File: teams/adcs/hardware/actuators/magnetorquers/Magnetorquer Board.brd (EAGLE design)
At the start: 90 x 90 mm, 29 parts

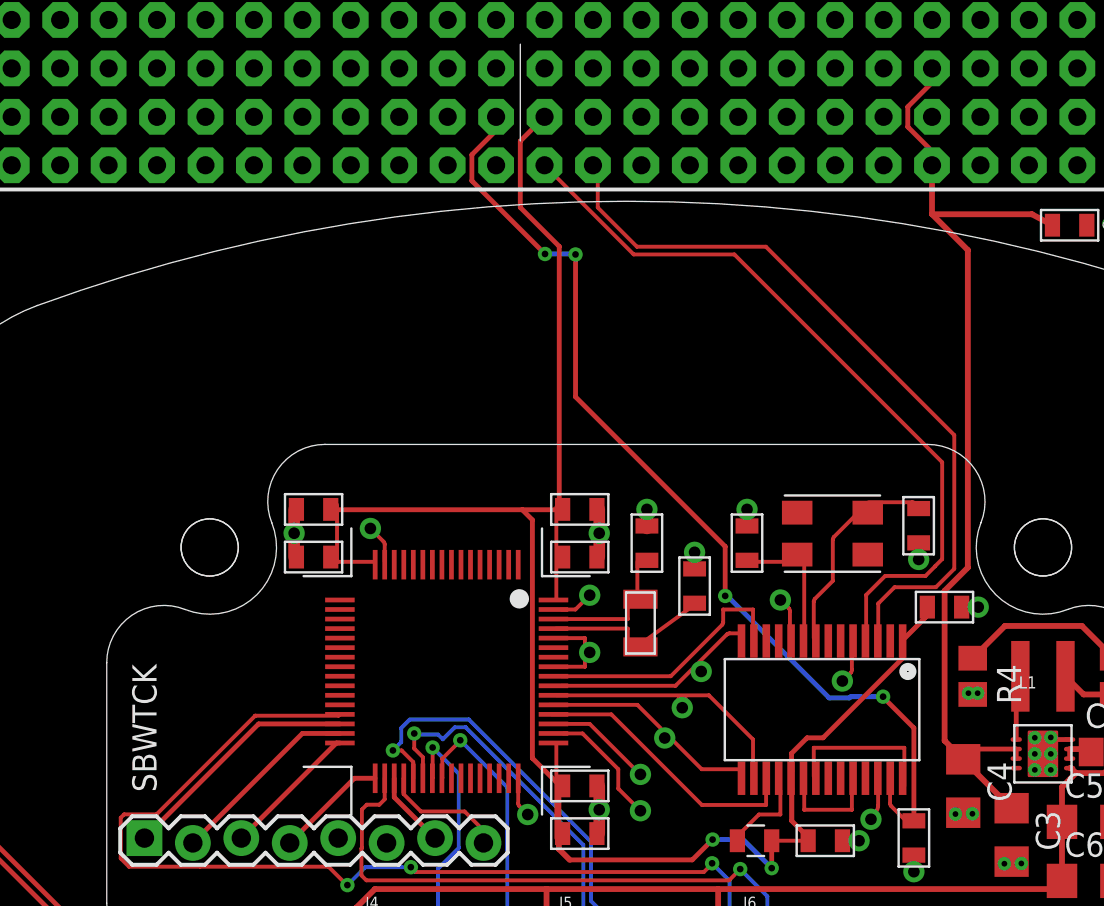
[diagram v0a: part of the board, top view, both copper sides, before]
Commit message: ADCS/MT: Switched from distributed 3V3/5V to LDOs
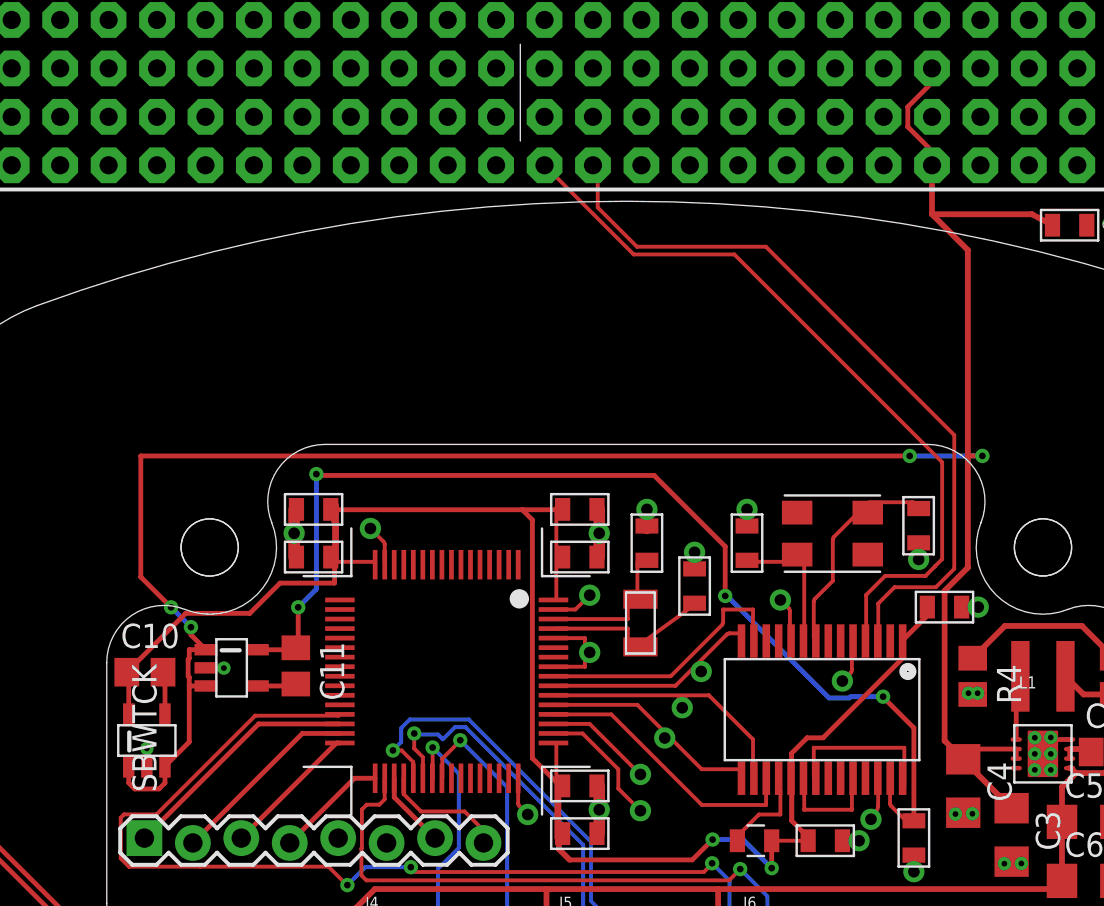
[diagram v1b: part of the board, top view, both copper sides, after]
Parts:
- added C10, C11: 0.01 μF, rcl:C0805
- added LDO_3V3, LDO_5V: LINEAR_LDO_LT1761-X, DubSat1 Components:SOT-23-5
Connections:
- removed net N$23: U$1.P$50, U$7.5V
- removed net N$24: U$1.P$54, U$7.3.3V@CAN1, U$7.3.3V@CAN2, U$7.3.3V@MSP1, U$7.3.3V@MSP2, U$7.3.3V_ANALOG@MSP2
- new net +3V3: C10.1, LDO_3V3.P$5, U$7.3.3V@CAN1, U$7.3.3V@CAN2, U$7.3.3V@MSP1, U$7.3.3V@MSP2, U$7.3.3V_ANALOG@MSP2
- new net +5V: C11.1, LDO_5V.P$5, U$7.5V
- new net N$26: C10.2, LDO_3V3.P$4
- new net N$33: C11.2, LDO_5V.P$4
- net GND: now also LDO_3V3.P$2, LDO_5V.P$2
- net N$19: now also LDO_3V3.P$1, LDO_3V3.P$3, LDO_5V.P$1, LDO_5V.P$3
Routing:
- net N$24: track 82.3 -> 0.08 mm, vias 2 -> 0
- net +3V3: track 0.00 -> 79.2 mm, vias 0 -> 2
- net N$19: track 53.2 -> 122.0 mm, vias 0 -> 4
- net +5V: track 0.00 -> 54.7 mm, vias 0 -> 4
- net N$23: track 49.6 -> 0.00 mm, vias 4 -> 0
- net N$26: track 0.00 -> 2.27 mm
- net N$33: track 0.00 -> 2.06 mm
- net GND: track 27.0 -> 28.9 mm, vias 37 -> 39

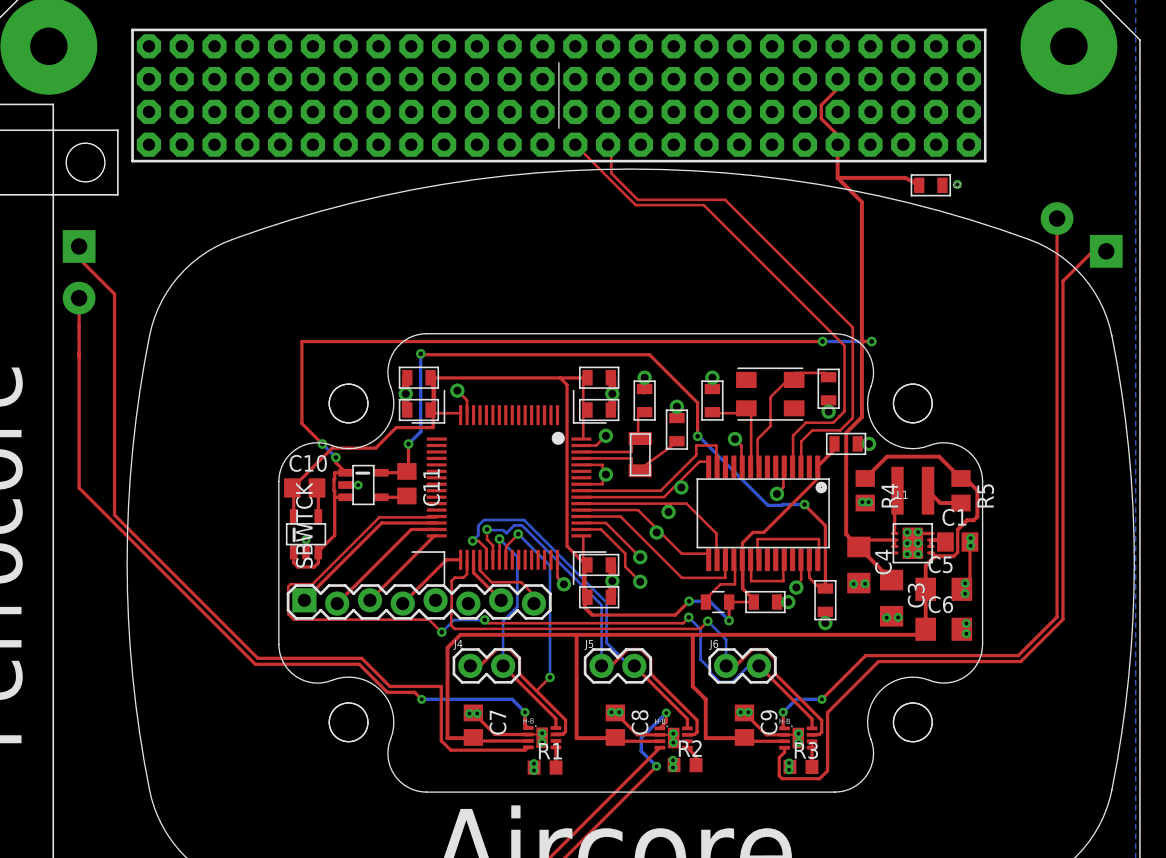
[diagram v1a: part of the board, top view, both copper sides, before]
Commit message: ADCS/MT: Routed LDOs and cleaned up schematic
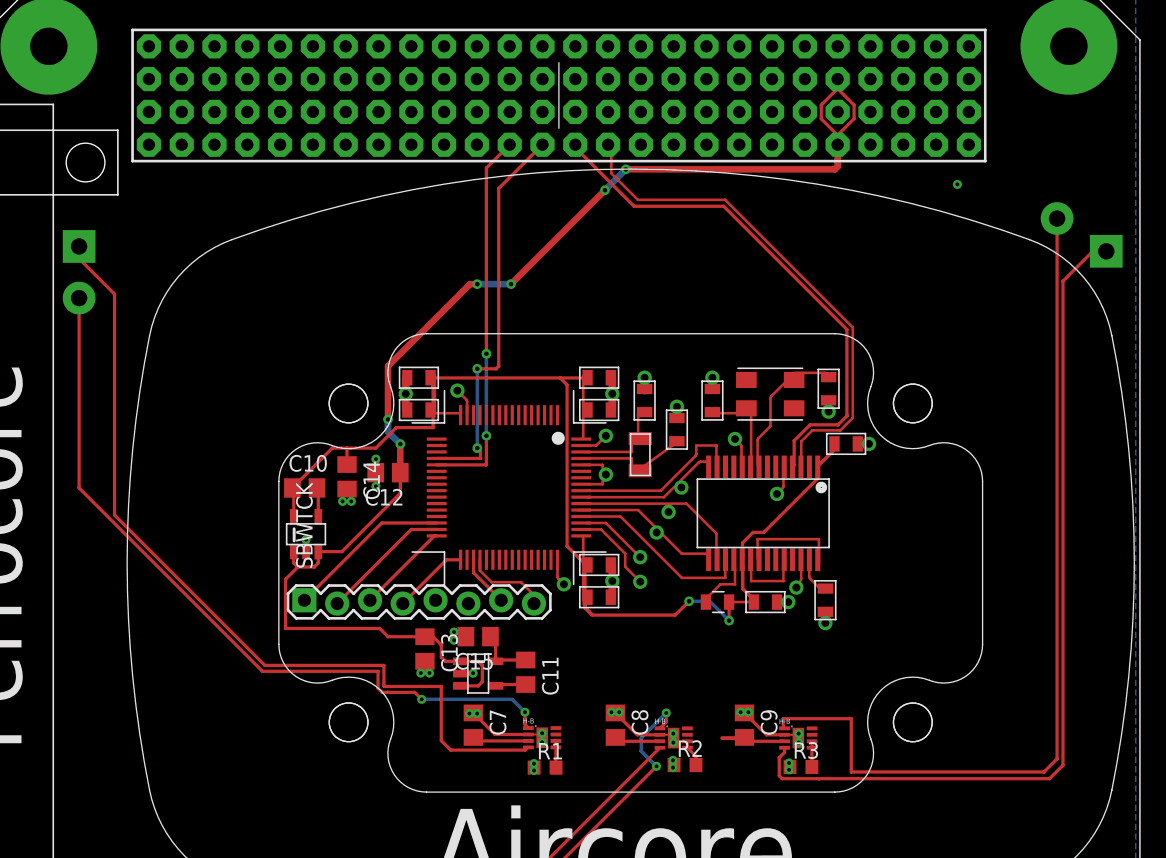
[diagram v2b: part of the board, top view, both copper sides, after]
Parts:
- removed C1: 2.2uF, rcl:C0805
- removed C2: 10uF, SparkFun-Capacitors:0805
- removed C3, C4, C6: 22uF, rcl:C1206
- removed C5: 47uF, rcl:C1206
- removed J4, J5, J6: (no value), SparkFun-Connectors:1X02
- removed L1: (no value), inductors:COILCRAFT
- removed R4: 120K, rcl:R0805
- removed R5: 680K, rcl:R0805
- removed U$6: LINEAR_BUCK_LTC3624, ICs:8-LFCSP
- added C12, C13: 1 μF, rcl:C0805
- added C14, C15: 10 μF, rcl:C0805
- moved C11 17.3 mm to (53.8, 34.7)
- moved LDO_5V 17.1 mm to (50.2, 34.6)
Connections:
- net N$21 renamed CANH
- net N$22 renamed CANL
- removed net N$16: C5.1, C6.1, C7.2, C8.2, C9.2, R4.1, R5.1, U$6.P$5, U1.VDD, U2.VDD, U3.VDD
- removed net N$17: C1.1, U$6.P$6, U$6.P$7
- removed net N$19: C2.1, C3.1, C4.1, LDO_3V3.P$1, LDO_3V3.P$3, LDO_5V.P$1, LDO_5V.P$3, U$1.P$85, U$1.P$87, U$6.P$2, U$6.P$3
- removed net N$20: L1.1, U$6.P$1
- removed net N$25: L1.2, R5.2
- removed net N$3: J4.1, U$7.P1.7_GPIO/PWM, U1.IN1
- removed net N$4: J5.1, U$7.P3.7_GPIO/PWM, U2.IN1
- removed net N$5: J6.1, U$7.P2.2_GPIO/PWM, U3.IN1
- removed net N$6: J6.2, U$7.P2.6_GPIO/PWM, U3.IN2
- removed net N$8: J5.2, U$7.P3.6_GPIO/PWM, U2.IN2
- removed net N$9: J4.2, U$7.P1.6_GPIO/PWM, U1.IN2
- new net 6V: C7.2, C8.2, C9.2, U1.VDD, U2.VDD, U3.VDD
- new net PWM_X_1: U$7.P1.7_GPIO/PWM, U2.IN1
- new net PWM_X_2: U$7.P1.6_GPIO/PWM, U2.IN2
- new net PWM_Y_1: U$7.P3.7_GPIO/PWM, U1.IN1
- new net PWM_Y_2: U$7.P3.6_GPIO/PWM, U1.IN2
- new net PWM_Z_1: U$7.P2.2_GPIO/PWM, U3.IN1
- new net PWM_Z_2: U$7.P2.6_GPIO/PWM, U3.IN2
- new net SYNC1: U$1.P$45, U$7.P7.2_SYNC1
- new net SYNC2: U$1.P$49, U$7.PJ.3_SYNC2
- new net VBAT: C12.1, C13.1, LDO_3V3.P$1, LDO_3V3.P$3, LDO_5V.P$1, LDO_5V.P$3, U$1.P$85, U$1.P$87
- net +3V3: now also C14.1
- net +5V: now also C15.1
- net GND: now also C12.2, C13.2, C14.2, C15.2; no longer C1.2, C2.2, C3.2, C4.2, C5.2, C6.2, R4.2, U$6.P$8, U$6.P$9
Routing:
- net N$19: track 122.0 -> 0.00 mm, vias 4 -> 0
- net N$16: track 104.9 -> 0.00 mm
- net VBAT: track 0.00 -> 103.2 mm, vias 0 -> 6
- net N$6: track 64.3 -> 0.00 mm, vias 3 -> 0
- net +5V: track 54.7 -> 4.45 mm, vias 4 -> 0
- net N$5: track 42.9 -> 0.00 mm, vias 1 -> 0
- net N$4: track 31.7 -> 0.00 mm, vias 1 -> 0
- net SYNC2: track 0.00 -> 30.7 mm, vias 0 -> 2
- net SYNC1: track 0.00 -> 29.4 mm, vias 0 -> 2
- net N$8: track 28.8 -> 0.00 mm, vias 1 -> 0
- net N$3: track 28.6 -> 0.00 mm, vias 2 -> 0
- net N$9: track 19.0 -> 0.00 mm, vias 1 -> 0
- net 6V: track 0.00 -> 13.0 mm
- net N$14: track 56.4 -> 68.4 mm, vias 2 -> 0
- net GND: track 28.9 -> 23.5 mm, vias 39 -> 29
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
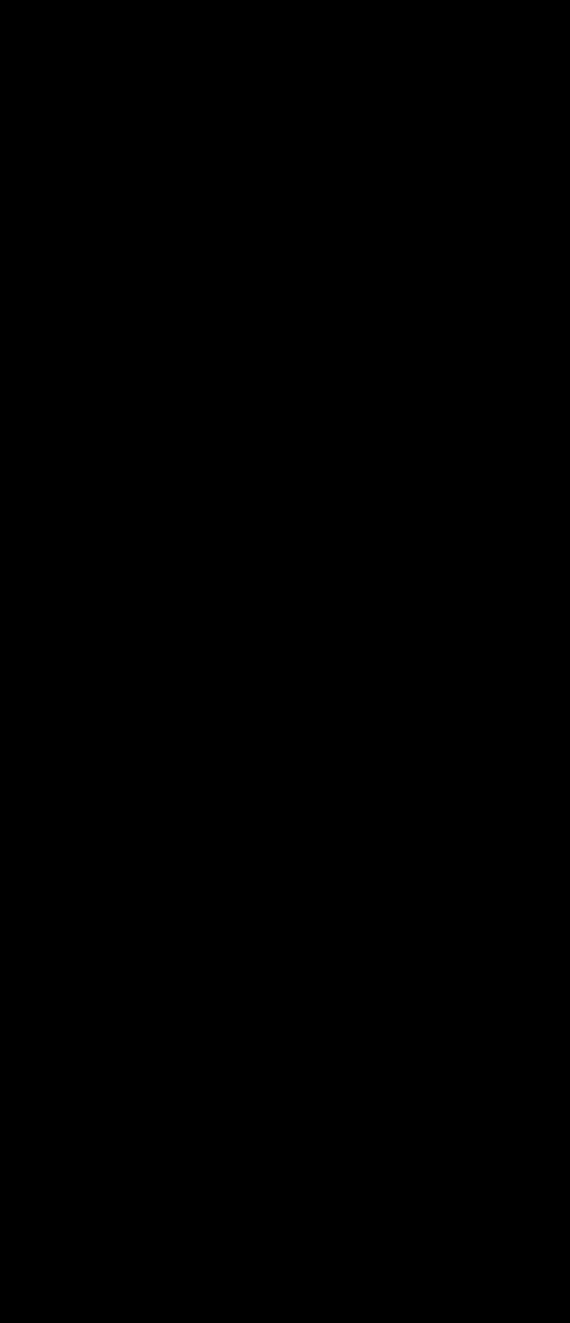
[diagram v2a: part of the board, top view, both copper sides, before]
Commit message: ADCS/MT: Start building SEPIC converter topology
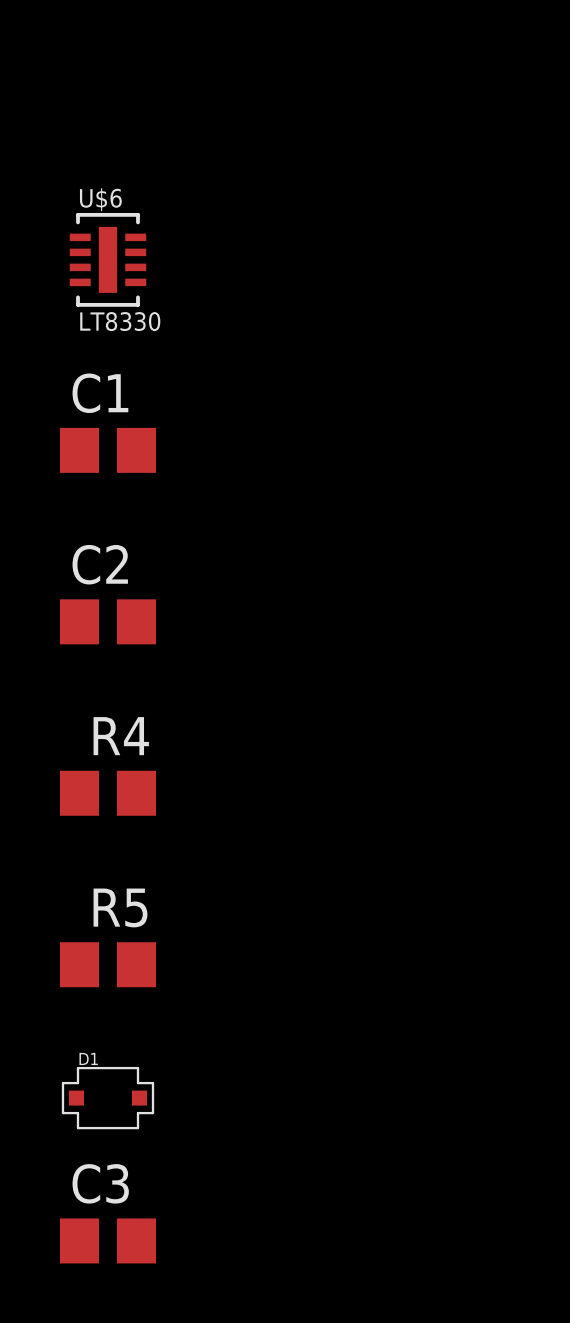
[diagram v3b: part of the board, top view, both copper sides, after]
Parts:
- added C1, C2, C3: (no value), rcl:C0805
- added D1: PMEG6010CEJ, DubSat1 Components:SC-90
- added R4, R5: (no value), rcl:R0805
- added U$6: LT8330, DubSat1 Components:DDB
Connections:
- new net N$3: D1.P$2, U$6.P$3, U$6.P$4
- new net N$4: C2.1, U$6.P$7
- new net N$5: R4.2, R5.1, U$6.P$8
- net 6V: now also C3.1, D1.P$1
- net GND: now also C1.2, C2.2, C3.2, R5.2, U$6.GND, U$6.P$5
- net VBAT: now also C1.1, R4.1, U$6.P$6
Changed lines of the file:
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@@
 <element name="C14" library="rcl" library_urn="urn:adsk.eagle:library:334" package="C0805" package3d_urn="urn:adsk.eagle:package:23617/2" value="10 μF" x="40.005" y="49.8475" rot="R270"/>
 <element name="C15" library="rcl" library_urn="urn:adsk.eagle:library:334" package="C0805" package3d_urn="urn:adsk.eagle:package:23617/2" value="10 μF" x="50.165" y="37.465" rot="R180"/>
+<element name="U$6" library="DubSat1 Components" package="DDB" value="LT8330" x="-22.86" y="-30.1625"/>
+<element name="C1" library="rcl" library_urn="urn:adsk.eagle:library:334" package="C0805" package3d_urn="urn:adsk.eagle:package:23617/2" value="" x="-22.86" y="-36.5125"/>
+<element name="C2" library="rcl" library_urn="urn:adsk.eagle:library:334" package="C0805" package3d_urn="urn:adsk.eagle:package:23617/2" value="" x="-22.86" y="-42.2275"/>
+<element name="R4" library="rcl" library_urn="urn:adsk.eagle:library:334" package="R0805" package3d_urn="urn:adsk.eagle:package:23553/2" value="" x="-22.86" y="-47.9425"/>
+<element name="R5" library="rcl" library_urn="urn:adsk.eagle:library:334" package="R0805" package3d_urn="urn:adsk.eagle:package:23553/2" value="" x="-22.86" y="-53.6575"/>
+<element name="D1" library="DubSat1 Components" package="SC-90" value="PMEG6010CEJ" x="-22.86" y="-58.1025"/>
+<element name="C3" library="rcl" library_urn="urn:adsk.eagle:library:334" package="C0805" package3d_urn="urn:adsk.eagle:package:23617/2" value="" x="-22.86" y="-62.865"/>
 </elements>
 <signals>
@@
 <via x="42.2402" y="51.2191" extent="1-16" drill="0.3" shape="square"/>
 <via x="42.2402" y="49.1109" extent="1-16" drill="0.3" shape="square"/>
+<contactref element="U$6" pad="P$5"/>
+<contactref element="U$6" pad="GND"/>
+<contactref element="C1" pad="2"/>
+<contactref element="C2" pad="2"/>
+<contactref element="R5" pad="2"/>
+<contactref element="C3" pad="2"/>
 <wire x1="74.9808" y1="29.8282125" x2="74.9554" y2="29.6164" width="0" layer="19" extent="1-1"/>
 <wire x1="65.331878125" y1="27.523078125" x2="65.2526" y2="27.3304" width="0" layer="19" extent="1-1"/>
@@
 <wire x1="49.215" y1="37.465" x2="48.2967" y2="37.1893" width="0" layer="19" extent="1-1"/>
 <wire x1="42.23" y1="50.165" x2="42.2402" y2="49.1109" width="0" layer="19" extent="1-1"/>
+<wire x1="-21.935" y1="-30.9125" x2="45.7186" y2="34.6493" width="0" layer="19" extent="1-1"/>
+<wire x1="-22.86" y1="-30.1625" x2="-21.935" y2="-30.9125" width="0" layer="19" extent="1-1"/>
+<wire x1="-21.91" y1="-36.5125" x2="-21.935" y2="-30.9125" width="0" layer="19" extent="1-1"/>
+<wire x1="-21.91" y1="-42.2275" x2="-21.91" y2="-36.5125" width="0" layer="19" extent="1-1"/>
+<wire x1="-21.91" y1="-53.6575" x2="-21.91" y2="-42.2275" width="0" layer="19" extent="1-1"/>
+<wire x1="-21.91" y1="-62.865" x2="-21.91" y2="-53.6575" width="0" layer="19" extent="1-1"/>
 </signal>
 <signal name="N$18">
@@
 <wire x1="49.7874" y1="29.6624" x2="50.058" y2="29.3918" width="0.254" layer="1"/>
 <wire x1="50.058" y1="29.3918" x2="54.053" y2="29.3918" width="0.254" layer="1"/>
+<contactref element="D1" pad="P$1"/>
+<contactref element="C3" pad="1"/>
 <wire x1="64.2384" y1="29.3664" x2="69.0574" y2="29.6124" width="0" layer="19" extent="1-1"/>
 <wire x1="54.053" y1="29.3918" x2="60.7874" y2="29.6624" width="0" layer="19" extent="1-1"/>
+<wire x1="-23.91" y1="-58.1025" x2="50.058" y2="29.3918" width="0" layer="19" extent="1-1"/>
+<wire x1="-23.81" y1="-62.865" x2="-23.91" y2="-58.1025" width="0" layer="19" extent="1-1"/>
 </signal>
 <signal name="VBAT">
@@
 <wire x1="44.1325" y1="48.5775" x2="44.1325" y2="50.1625" width="0.254" layer="1"/>
 <wire x1="44.1325" y1="50.1625" x2="44.13" y2="50.165" width="0.254" layer="1"/>
+<contactref element="U$6" pad="P$6"/>
+<contactref element="C1" pad="1"/>
+<contactref element="R4" pad="1"/>
+<wire x1="-21.935" y1="-30.4125" x2="35.2425" y2="38.1" width="0" layer="19" extent="1-1"/>
+<wire x1="-23.81" y1="-36.5125" x2="-21.935" y2="-30.4125" width="0" layer="19" extent="1-1"/>
+<wire x1="-23.81" y1="-47.9425" x2="-23.81" y2="-36.5125" width="0" layer="19" extent="1-1"/>
 </signal>
 <signal name="N$1">
@@
 <wire x1="50.8" y1="73.7646" x2="52.6034" y2="75.568" width="0.254" layer="1"/>
 </signal>
+<signal name="N$4">
+<contactref element="U$6" pad="P$7"/>
+<contactref element="C2" pad="1"/>
+<wire x1="-21.935" y1="-29.9125" x2="-23.81" y2="-42.2275" width="0" layer="19" extent="1-1"/>
+</signal>
+<signal name="N$5">
+<contactref element="U$6" pad="P$8"/>
+<contactref element="R5" pad="1"/>
+<contactref element="R4" pad="2"/>
+<wire x1="-21.91" y1="-47.9425" x2="-23.81" y2="-53.6575" width="0" layer="19" extent="1-1"/>
+<wire x1="-21.935" y1="-29.4125" x2="-21.91" y2="-47.9425" width="0" layer="19" extent="1-1"/>
+</signal>
+<signal name="N$3">
+<contactref element="U$6" pad="P$3"/>
+<contactref element="D1" pad="P$2"/>
+<contactref element="U$6" pad="P$4"/>
+<wire x1="-23.785" y1="-30.9125" x2="-21.81" y2="-58.1025" width="0" layer="19" extent="1-1"/>
+<wire x1="-23.785" y1="-30.4125" x2="-23.785" y2="-30.9125" width="0" layer="19" extent="1-1"/>
+</signal>
 </signals>
